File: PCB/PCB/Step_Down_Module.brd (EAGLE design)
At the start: 68 x 99.2 mm, 42 parts, among them Q1 TPH2900ENH

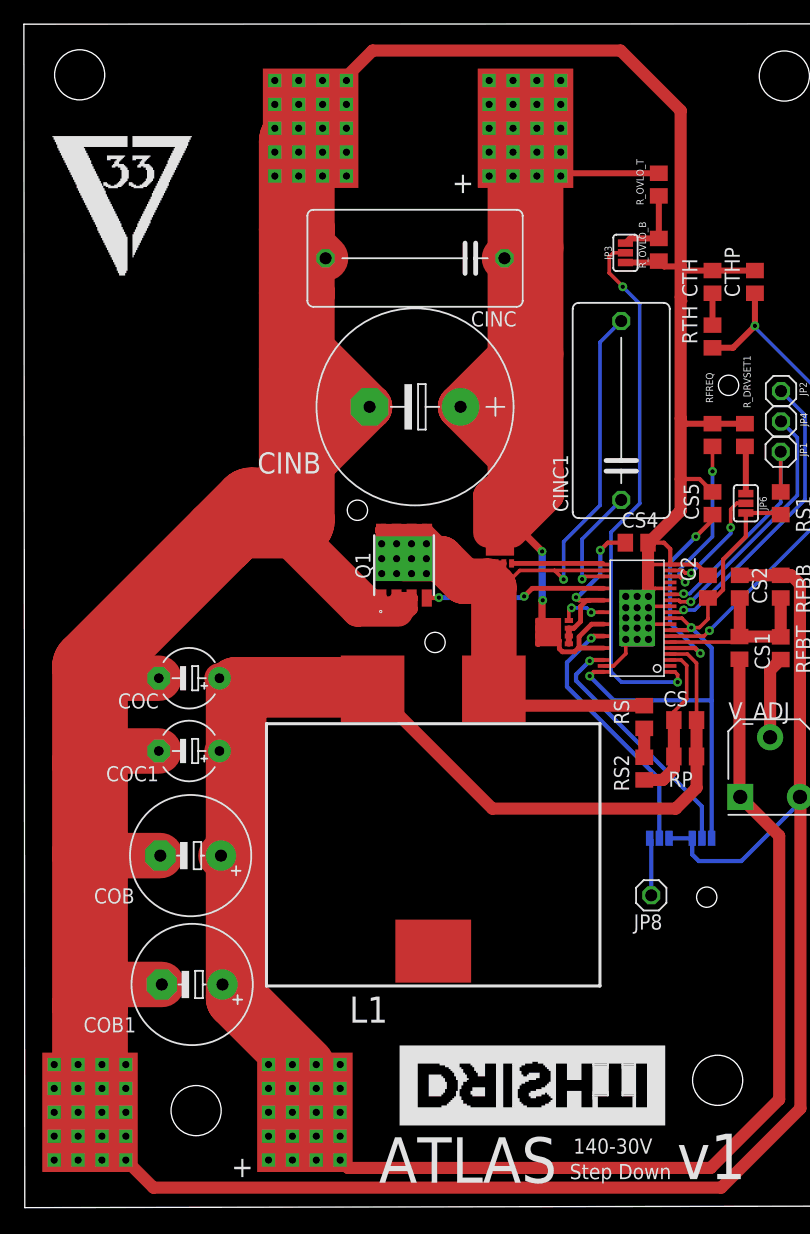
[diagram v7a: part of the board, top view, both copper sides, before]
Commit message: PCB Routing edits - moved bypass cap, changed trace widths
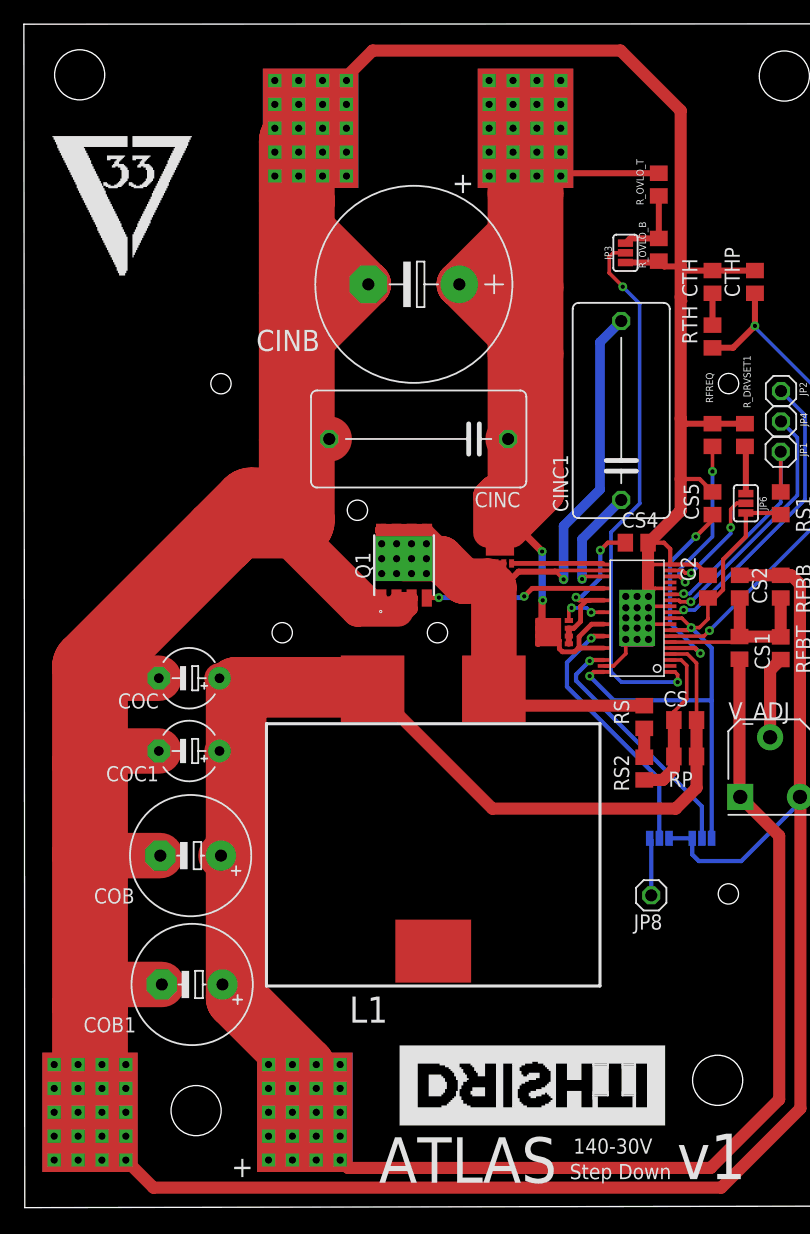
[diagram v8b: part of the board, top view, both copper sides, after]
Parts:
- moved CINC 15.1 mm to (33.1, 64.0)
- moved CINB 10.3 mm to (32.7, 76.9)
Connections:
- net GND: now also U$5.NEG1, U$7.NEG1
- net VIN: now also U$5.POS1
- net VOUT: now also U$7.POS1
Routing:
- net VIN: track 97.7 -> 112.0 mm
- net VOUT: track 178.9 -> 184.1 mm
